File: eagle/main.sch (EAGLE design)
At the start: 33 parts, among them IC1 STM32F103, IC2 LM1117, Q1 8MHz

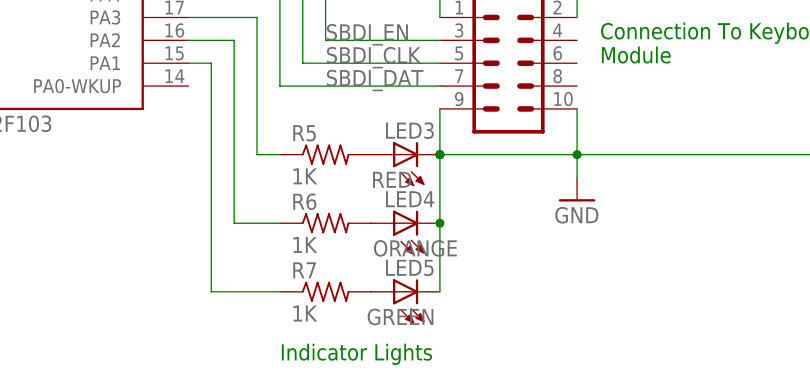
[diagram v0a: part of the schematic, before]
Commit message: Add silkscreen labels
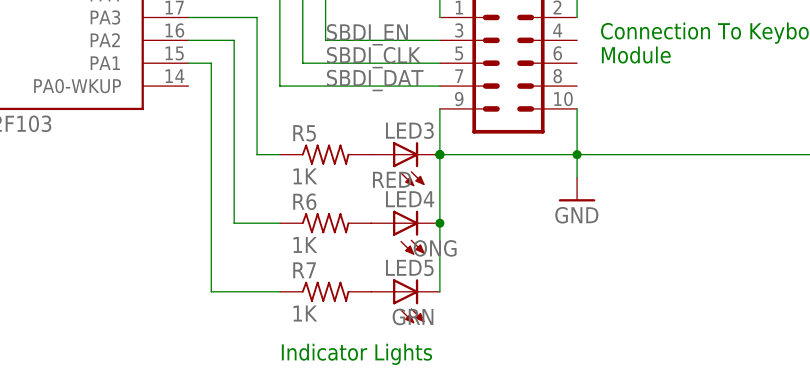
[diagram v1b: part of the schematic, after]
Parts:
- LED4: value ORANGE -> ONG
- LED5: value GREEN -> GRN
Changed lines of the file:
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@@
 <part name="P+8" library="supply1" library_urn="urn:adsk.eagle:library:371" deviceset="VCC" device=""/>
 <part name="LED3" library="led" library_urn="urn:adsk.eagle:library:259" deviceset="LED" device="5MM" package3d_urn="urn:adsk.eagle:package:15799/2" value="RED"/>
-<part name="LED4" library="led" library_urn="urn:adsk.eagle:library:259" deviceset="LED" device="5MM" package3d_urn="urn:adsk.eagle:package:15799/2" value="ORANGE"/>
+<part name="LED4" library="led" library_urn="urn:adsk.eagle:library:259" deviceset="LED" device="5MM" package3d_urn="urn:adsk.eagle:package:15799/2" value="ONG"/>
 <part name="R5" library="rcl" library_urn="urn:adsk.eagle:library:334" deviceset="R-US_" device="0204/7" package3d_urn="urn:adsk.eagle:package:23498/1" value="1K"/>
 <part name="R6" library="rcl" library_urn="urn:adsk.eagle:library:334" deviceset="R-US_" device="0204/7" package3d_urn="urn:adsk.eagle:package:23498/1" value="1K"/>
 <part name="R7" library="rcl" library_urn="urn:adsk.eagle:library:334" deviceset="R-US_" device="0204/7" package3d_urn="urn:adsk.eagle:package:23498/1" value="1K"/>
-<part name="LED5" library="led" library_urn="urn:adsk.eagle:library:259" deviceset="LED" device="5MM" package3d_urn="urn:adsk.eagle:package:15799/2" value="GREEN"/>
+<part name="LED5" library="led" library_urn="urn:adsk.eagle:library:259" deviceset="LED" device="5MM" package3d_urn="urn:adsk.eagle:package:15799/2" value="GRN"/>
 <part name="S1" library="switch-misc" library_urn="urn:adsk.eagle:library:376" deviceset="PVA2R" device="" package3d_urn="urn:adsk.eagle:package:27428/1"/>
 <part name="U1" library="SparkFun-Connectors" library_urn="urn:adsk.eagle:library:513" deviceset="USB_AB" device="_SMT" package3d_urn="urn:adsk.eagle:package:38266/1"/>

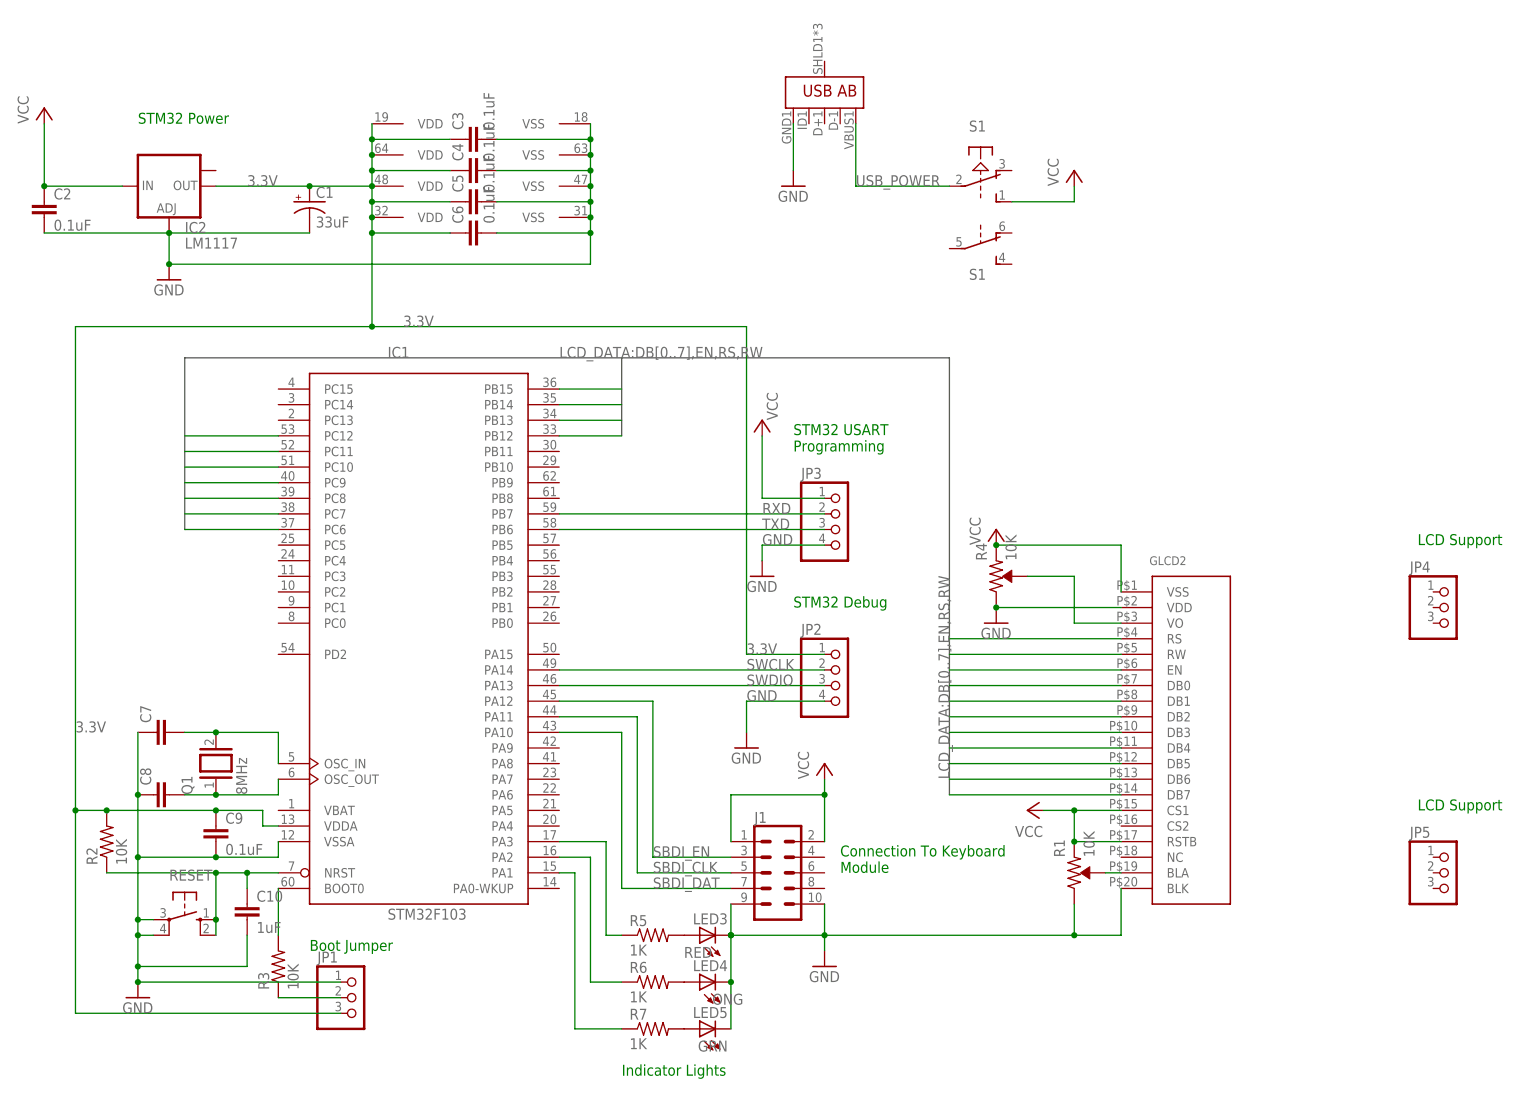
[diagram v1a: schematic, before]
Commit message: Fix errors in main module schematic
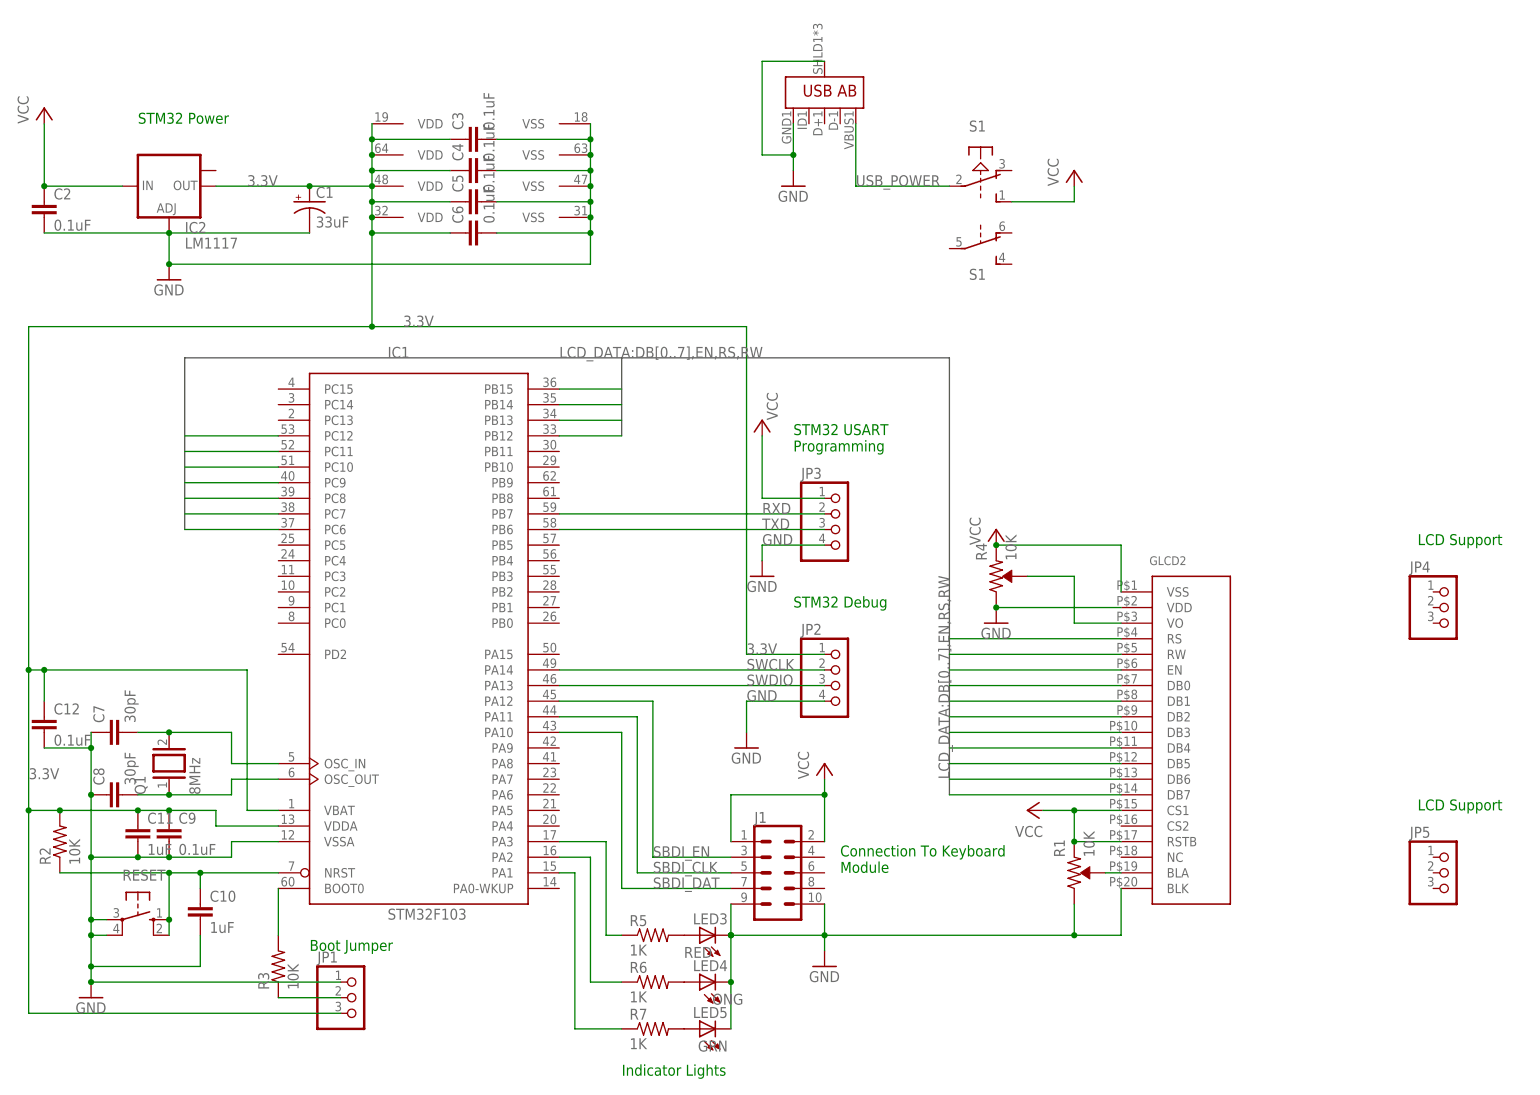
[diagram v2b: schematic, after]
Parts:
- added C11: 1uF, rcl:C-EU025-025X050
- added C12: 0.1uF, rcl:C-EU025-025X050
- C7, C8: value (none) -> 30pF
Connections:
- net 3.3V: now also C11.1, C12.1, IC1MCU.VBAT
- net GND: now also C11.2, C12.2, U1.SHIELD
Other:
- moved on the sheet: C10, C7, C8, C9, Q1, R2, RESET

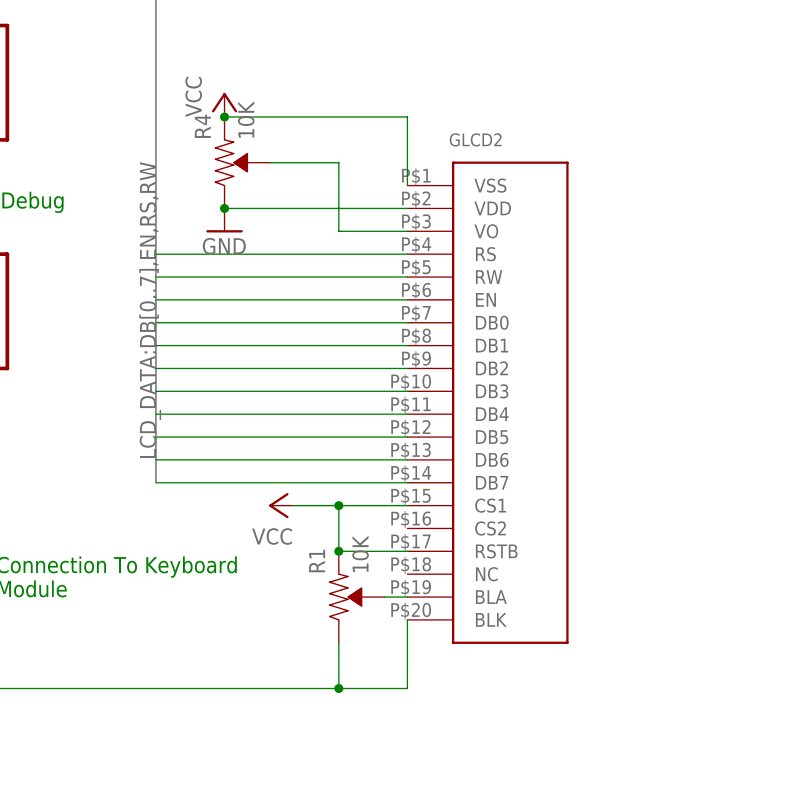
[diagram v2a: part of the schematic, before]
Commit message: Partially fix error with LCD library in main board
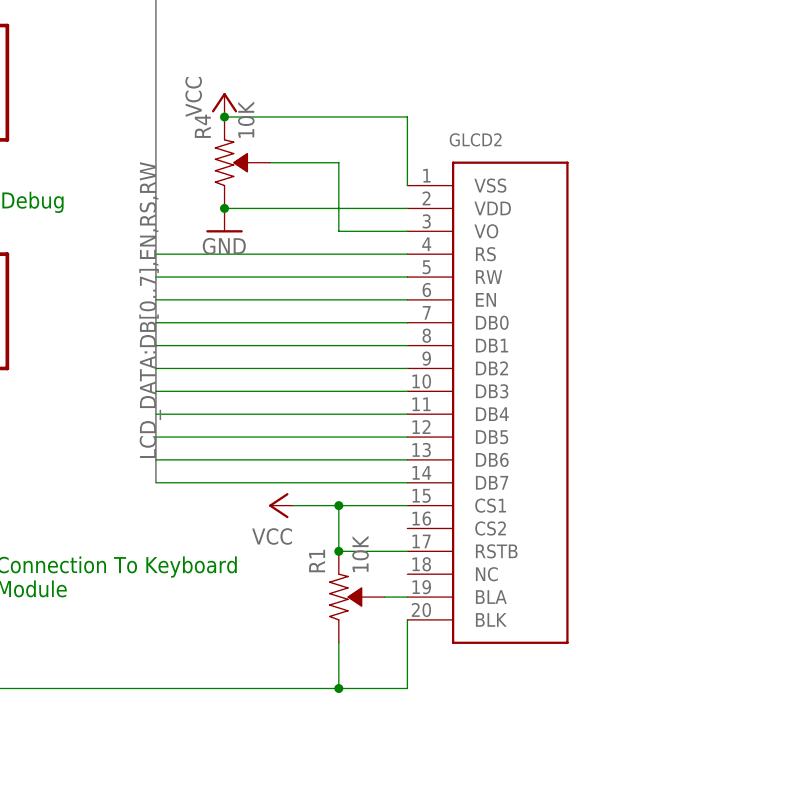
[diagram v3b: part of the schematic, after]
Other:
- moved on the sheet: GLCD2

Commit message: Re-route LCD to fix errors
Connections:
- net DB0: now also IC1MCU.PB12; no longer IC1MCU.PC9
- net DB1: now also IC1MCU.PB13; no longer IC1MCU.PC8
- net DB2: now also IC1MCU.PB14; no longer IC1MCU.PC7
- net DB3: now also IC1MCU.PB15; no longer IC1MCU.PC6
- net DB4: now also IC1MCU.PC6; no longer IC1MCU.PB15
- net DB5: now also IC1MCU.PC7; no longer IC1MCU.PB14
- net DB6: now also IC1MCU.PC8; no longer IC1MCU.PB13
- net DB7: now also IC1MCU.PC9; no longer IC1MCU.PB12
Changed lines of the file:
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@@
 </segment>
 <segment>
-<pinref part="IC1" gate="MCU" pin="PC9"/>
-<wire x1="-60.96" y1="22.86" x2="-76.2" y2="22.86" width="0.1524" layer="91"/>
+<pinref part="IC1" gate="MCU" pin="PB12"/>
+<wire x1="-15.24" y1="30.48" x2="-5.08" y2="30.48" width="0.1524" layer="91"/>
 </segment>
 </net>
@@
 </segment>
 <segment>
-<pinref part="IC1" gate="MCU" pin="PC8"/>
-<wire x1="-60.96" y1="20.32" x2="-76.2" y2="20.32" width="0.1524" layer="91"/>
+<pinref part="IC1" gate="MCU" pin="PB13"/>
+<wire x1="-15.24" y1="33.02" x2="-5.08" y2="33.02" width="0.1524" layer="91"/>
 </segment>
 </net>
@@
 </segment>
 <segment>
-<pinref part="IC1" gate="MCU" pin="PC7"/>
-<wire x1="-60.96" y1="17.78" x2="-76.2" y2="17.78" width="0.1524" layer="91"/>
+<pinref part="IC1" gate="MCU" pin="PB14"/>
+<wire x1="-15.24" y1="35.56" x2="-5.08" y2="35.56" width="0.1524" layer="91"/>
 </segment>
 </net>
@@
 </segment>
 <segment>
-<pinref part="IC1" gate="MCU" pin="PC6"/>
-<wire x1="-60.96" y1="15.24" x2="-76.2" y2="15.24" width="0.1524" layer="91"/>
+<pinref part="IC1" gate="MCU" pin="PB15"/>
+<wire x1="-15.24" y1="38.1" x2="-5.08" y2="38.1" width="0.1524" layer="91"/>
 </segment>
 </net>
@@
 </segment>
 <segment>
-<pinref part="IC1" gate="MCU" pin="PB15"/>
-<wire x1="-15.24" y1="38.1" x2="-5.08" y2="38.1" width="0.1524" layer="91"/>
+<pinref part="IC1" gate="MCU" pin="PC6"/>
+<wire x1="-60.96" y1="15.24" x2="-76.2" y2="15.24" width="0.1524" layer="91"/>
 </segment>
 </net>
@@
 </segment>
 <segment>
-<pinref part="IC1" gate="MCU" pin="PB14"/>
-<wire x1="-15.24" y1="35.56" x2="-5.08" y2="35.56" width="0.1524" layer="91"/>
+<pinref part="IC1" gate="MCU" pin="PC7"/>
+<wire x1="-60.96" y1="17.78" x2="-76.2" y2="17.78" width="0.1524" layer="91"/>
 </segment>
 </net>
@@
 </segment>
 <segment>
-<pinref part="IC1" gate="MCU" pin="PB13"/>
-<wire x1="-15.24" y1="33.02" x2="-5.08" y2="33.02" width="0.1524" layer="91"/>
+<pinref part="IC1" gate="MCU" pin="PC8"/>
+<wire x1="-60.96" y1="20.32" x2="-76.2" y2="20.32" width="0.1524" layer="91"/>
 </segment>
 </net>
@@
 </segment>
 <segment>
-<pinref part="IC1" gate="MCU" pin="PB12"/>
-<wire x1="-15.24" y1="30.48" x2="-5.08" y2="30.48" width="0.1524" layer="91"/>
+<pinref part="IC1" gate="MCU" pin="PC9"/>
+<wire x1="-60.96" y1="22.86" x2="-76.2" y2="22.86" width="0.1524" layer="91"/>
 </segment>
 </net>

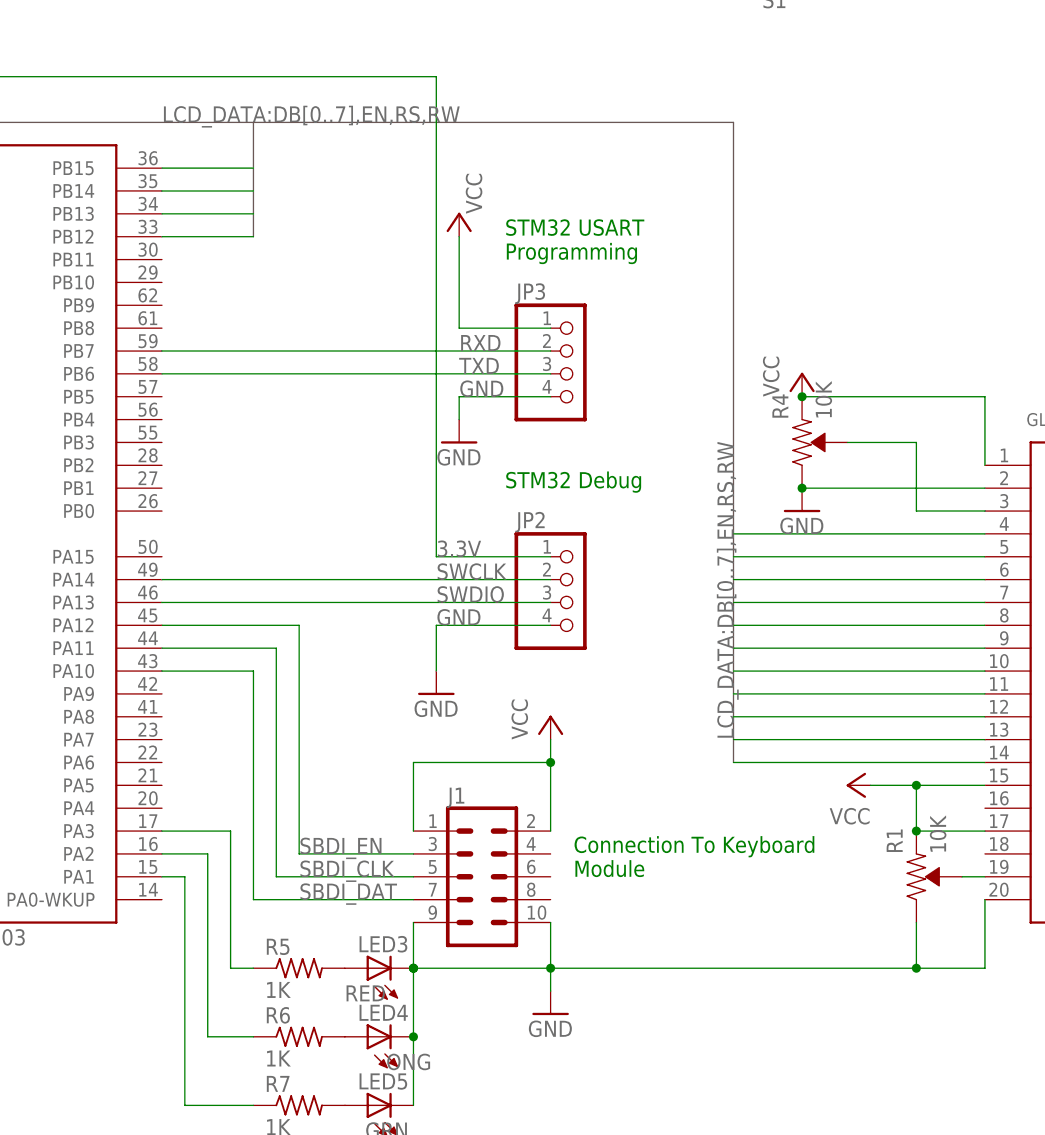
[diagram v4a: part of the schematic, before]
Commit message: Fix error in main schematic
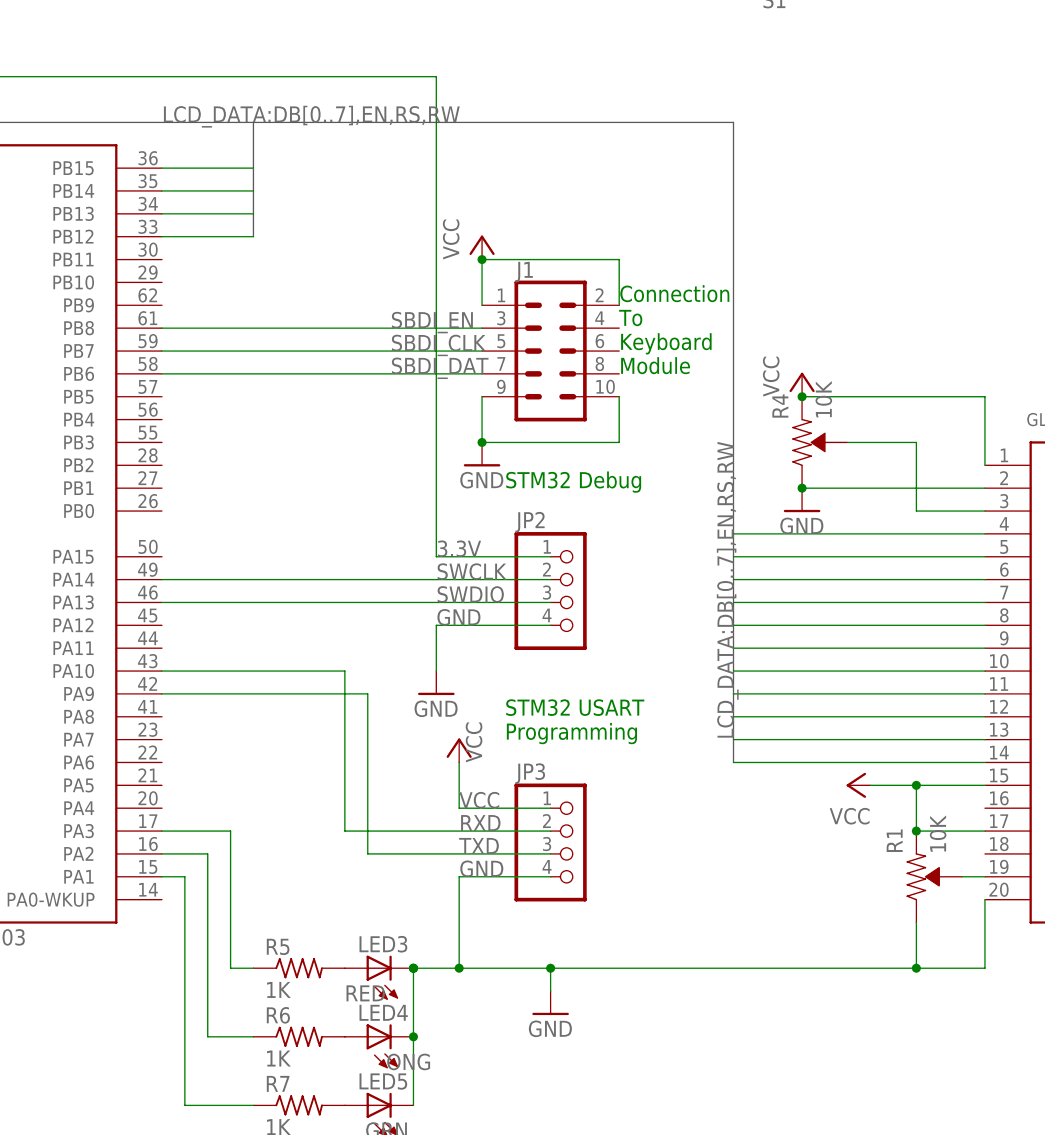
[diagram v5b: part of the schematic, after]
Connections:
- net RXD: now also IC1MCU.PA10; no longer IC1MCU.PB7
- net SBDI_CLK: now also IC1MCU.PB7; no longer IC1MCU.PA11
- net SBDI_DAT: now also IC1MCU.PB6; no longer IC1MCU.PA10
- net SBDI_EN: now also IC1MCU.PB8; no longer IC1MCU.PA12
- net TXD: now also IC1MCU.PA9; no longer IC1MCU.PB6
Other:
- moved on the sheet: J1, JP3
